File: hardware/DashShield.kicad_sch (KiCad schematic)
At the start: 60 parts, among them J1 GPIO, J2 Steering Wheel, J3 Dash LEDs, J4 CAN 0, J5 PWR, J6 CAN 1, Q1 2N7002, Q2 2N7002, Q3 2N7002, Q4 2N7002, Q5 2N7002, Q6 2N7002, U1 CAT24C256, U2 MCP2562-E-SN, U3 MCP2515-xST, U4 MCP2515-xST, U5 MCP2562-E-SN, Y1 8MHz, Y2 8MHz

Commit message: feat: finish power supply
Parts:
- added C14, C15, C16, C19: 10uF, symbol Device:C_Polarized
- added C17, C18: 100nF, symbol Device:C
- added C20: 10nF, symbol Device:C
- added D6: CRS15, Diode_SMD:D_SOD-123F, symbol Device:D
- added R18, R20, R21, R22: 10k, symbol Device:R
- added U6: ~, U3V40x:U3V40x, symbol U3V40x:U3V40F5
- R16: value 3.3Ω -> 3.3
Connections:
- net +5V: now also C15.1, C16.1, C17.1, C18.1, C19.1, C20.1, U6. (~{EN})
- net GND: now also C14.2, C15.2, C16.2, C17.2, C18.2, C19.2, C20.2, R18.1, R22.1, U6. (~{EN})
- net VS: now also C14.1, D6.1 (K), R20.2, U6. (~{EN})
- net +BATT: now reaches C12.1, D2.1 (K), D5.2 (A), R15.2, R16.1, R19.2
- net +BATT: now also D6.2 (A), R21.2
- new net VBATT Sense: R21.1, R22.2
- new net VIN Sense: R18.2, R20.1
- no-connect marks 15 -> 16
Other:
- note added: "Additional Decoupling Capacitors"
- note added: "Power Loss Detection"
- moved on the sheet: C12, C13, D1, D2, D3, D4, D5, J5, R15, R16, R17, R19

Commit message: feat: initial revision of dash PCB schematic
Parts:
- removed J4: CAN 0, symbol Connector_Generic_Shielded:Conn_01x02_Shielded
- removed J6: CAN 1, symbol Connector_Generic_Shielded:Conn_01x02_Shielded
- removed JP1: ID_WP, symbol Jumper:SolderJumper_2_Open
- added C21, C22: 10nF, Capacitor_SMD:C_0603_1608Metric, symbol Device:C
- added J4: CAN0, Connector_Molex:Molex_Micro-Fit_3.0_43650-0315_1x03_P3.00mm_Vertical, symbol Connector_Generic:Conn_01x03
- added J7: CAN1, Connector_Molex:Molex_Micro-Fit_3.0_43650-0315_1x03_P3.00mm_Vertical, symbol Connector_Generic:Conn_01x03
- added JP1: WP Enable Jumper, Connector_PinHeader_2.54mm:PinHeader_1x02_P2.54mm_Vertical, symbol Jumper:Jumper_2_Open
- added Q7, Q8, Q9: 2N7002, Package_TO_SOT_SMD:SOT-23, symbol Transistor_FET:2N7002
- added R23, R24, R25, R26, R27, R28: 270, Resistor_SMD:R_0603_1608Metric, symbol Device:R
- added R29, R30, R33: 1k, Resistor_SMD:R_0603_1608Metric, symbol Device:R
- added R31, R32, R35, R36, R37, R38, R39, R40: 10k, Resistor_SMD:R_0603_1608Metric, symbol Device:R
- C1, C10, C11, C14, C15, C16, C17, C18, C19, C2, C20, C3, C4, C5, C6, C7, C8, C9: footprint (none) -> Capacitor_SMD:C_0603_1608Metric
- C12, C13: value 10F -> 25F; footprint (none) -> Capacitor_THT:CP_Radial_D16.0mm_P7.50mm
- D1: footprint (none) -> Diode_SMD:D_SMA
- D2, D3: footprint (none) -> Package_TO_SOT_SMD:SOT-23
- D4: footprint (none) -> LED_SMD:LED_0603_1608Metric
- J2: footprint (none) -> Connector_Molex:Molex_Micro-Fit_3.0_43045-1212_2x06_P3.00mm_Vertical; symbol Connector_Generic:Conn_02x06_Counter_Clockwise -> Connector_Generic:Conn_02x06_Top_Bottom
- J3: footprint (none) -> Connector_Molex:Molex_Micro-Fit_3.0_43045-0812_2x04_P3.00mm_Vertical; symbol Connector_Generic:Conn_02x04_Counter_Clockwise -> Connector_Generic:Conn_02x04_Top_Bottom
- J5: footprint (none) -> Connector_Molex:Molex_Micro-Fit_3.0_43650-0215_1x02_P3.00mm_Vertical
- JP2, JP3, JP4, JP5: footprint (none) -> Connector_PinHeader_2.54mm:PinHeader_1x02_P2.54mm_Vertical
- R1, R10, R11, R12, R13, R14, R15, R16, R17, R19, R2, R20, R21, R3, R4, R5, R6, R7, R8, R9: footprint (none) -> Resistor_SMD:R_0603_1608Metric
- R18, R22: value 10k -> 20k; footprint (none) -> Resistor_SMD:R_0603_1608Metric
- U1: footprint (none) -> Package_SO:SOIC-8_3.9x4.9mm_P1.27mm
- Y1, Y2: footprint (none) -> Crystal:Crystal_SMD_HC49-SD
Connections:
- net GPIO12/PWM0 is gone; now on net FAST 2: J1.32 (Pin_32)
- net GPIO24 is gone; now on net CAN0 INT: J1.18 (Pin_18)
- net GPIO25 is gone; now on net CAN1 INT: J1.22 (Pin_22)
- net GPIO5 is gone; now on net FAST 0: J1.29 (Pin_29)
- net GPIO6 is gone; now on net FAST 1: J1.31 (Pin_31)
- net SLOW 0 is gone; now on net GPIO26: Q1.1 (G)
- net SLOW 1 is gone; now on net GPIO19/PCM.FS: Q2.1 (G)
- net SLOW 2 is gone; now on net GPIO13/PWM1: Q3.1 (G)
- net VBATT Sense is gone; now on net GPIO2/SDA1: R21.1, R22.2
- net VIN Sense is gone; now on net GPIO3/SCL1: R18.2, R20.1
- net +3.3V: now also J2.7 (Pin_7)
- net +3V3: now also R33.1
- net +5V: now also J3.5 (Pin_5), U6.4 (OUT); no longer J3.8 (Pin_8), U6. (~{EN})
- net +BATT: now also D2.3 (K); no longer D2.1 (K)
- net CAN0 High: now also J4.1 (Pin_1)
- net CAN0 Low: now also J4.2 (Pin_2)
- net CAN1 High: now also J7.1 (Pin_1)
- net CAN1 Low: now also J7.2 (Pin_2)
- net FAST LED 0: now also J3.6 (Pin_6); no longer J3.7 (Pin_7)
- net FAST LED 1: now also J3.7 (Pin_7); no longer J3.6 (Pin_6)
- net FAST LED 2: now also J3.8 (Pin_8); no longer J3.5 (Pin_5)
- net GND: now also D3.1 (A), U6.3 (GND), C21.2, C22.2, Q7.2 (S), Q8.2 (S), Q9.2 (S), R29.2, R30.2, R35.2, R37.2, R39.2; no longer D3.2 (A), U6. (~{EN})
- net GPIO16: now also R40.1
- net GPIO17: now also Q9.1 (G)
- net GPIO18/PCM.CLK: now also R31.1
- net GPIO20/PCM.DIN: now also R38.1
- net GPIO21/PCM.DOUT: now also R36.1
- net GPIO22: now also Q7.1 (G)
- net GPIO23: now also R32.1
- net GPIO27: now also Q8.1 (G)
- net GPIO2/SDA1: now also C22.1
- net GPIO3/SCL1: now also C21.1
- net VS: now also U6.2 (VIN); no longer U6. (~{EN})
- net at C12.2, C13.1, R15.1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: now also D2.1 (A), D3.3 (K); no longer D2.2 (A), D3.1 (K)
- net CAN0 Shield: now reaches JP3.2 (B)
- net CAN0 Shield: now also J4.3 (Pin_3)
- net at U1.7 (WP): now also JP1.1 (A)
- net TC LED 0: now reaches J2.1 (Pin_1)
- net TC LED 0: now also R23.1
- net TC Disable Button: now reaches J2.10 (Pin_10)
- net TC Disable Button: now also R39.1, R40.2
- net Radio Enable Button: now reaches J2.11 (Pin_11)
- net Radio Enable Button: now also R37.1, R38.2
- net Lap Marker Button: now reaches J2.12 (Pin_12)
- net Lap Marker Button: now also R35.1, R36.2
- net TC LED 1: now reaches J2.2 (Pin_2)
- net TC LED 1: now also R25.1
- net TC LED 2: now reaches J2.3 (Pin_3)
- net TC LED 2: now also R27.1
- net TC LED 3: now reaches J2.4 (Pin_4)
- net TC LED 3: now also R28.1
- net TC LED 4: now reaches J2.5 (Pin_5)
- net TC LED 4: now also R26.1
- net TC LED 5: now reaches J2.6 (Pin_6)
- net TC LED 5: now also R24.1
- net Wheel Slip Adjust Dial: now reaches J2.8 (Pin_8)
- net Wheel Slip Adjust Dial: now also R29.1, R31.2
- net TC Power Adjust Dial: now reaches J2.9 (Pin_9)
- net TC Power Adjust Dial: now also R30.1, R32.2
- net CAN1 Shield: now reaches JP4.2 (B)
- net CAN1 Shield: now also J7.3 (Pin_3)
- new net: Q8.3 (D), R25.2, R26.2
- new net: JP1.2 (B), R33.2
- new net: Q7.3 (D), R23.2, R24.2
- new net: Q9.3 (D), R27.2, R28.2
- no-connect marks 16 -> 19
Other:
- note added: "Steering Wheel Interface"
- moved on the sheet: C1, J1, J2, J3, Q1, Q2, Q3, Q4, Q5, Q6, R1, R2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

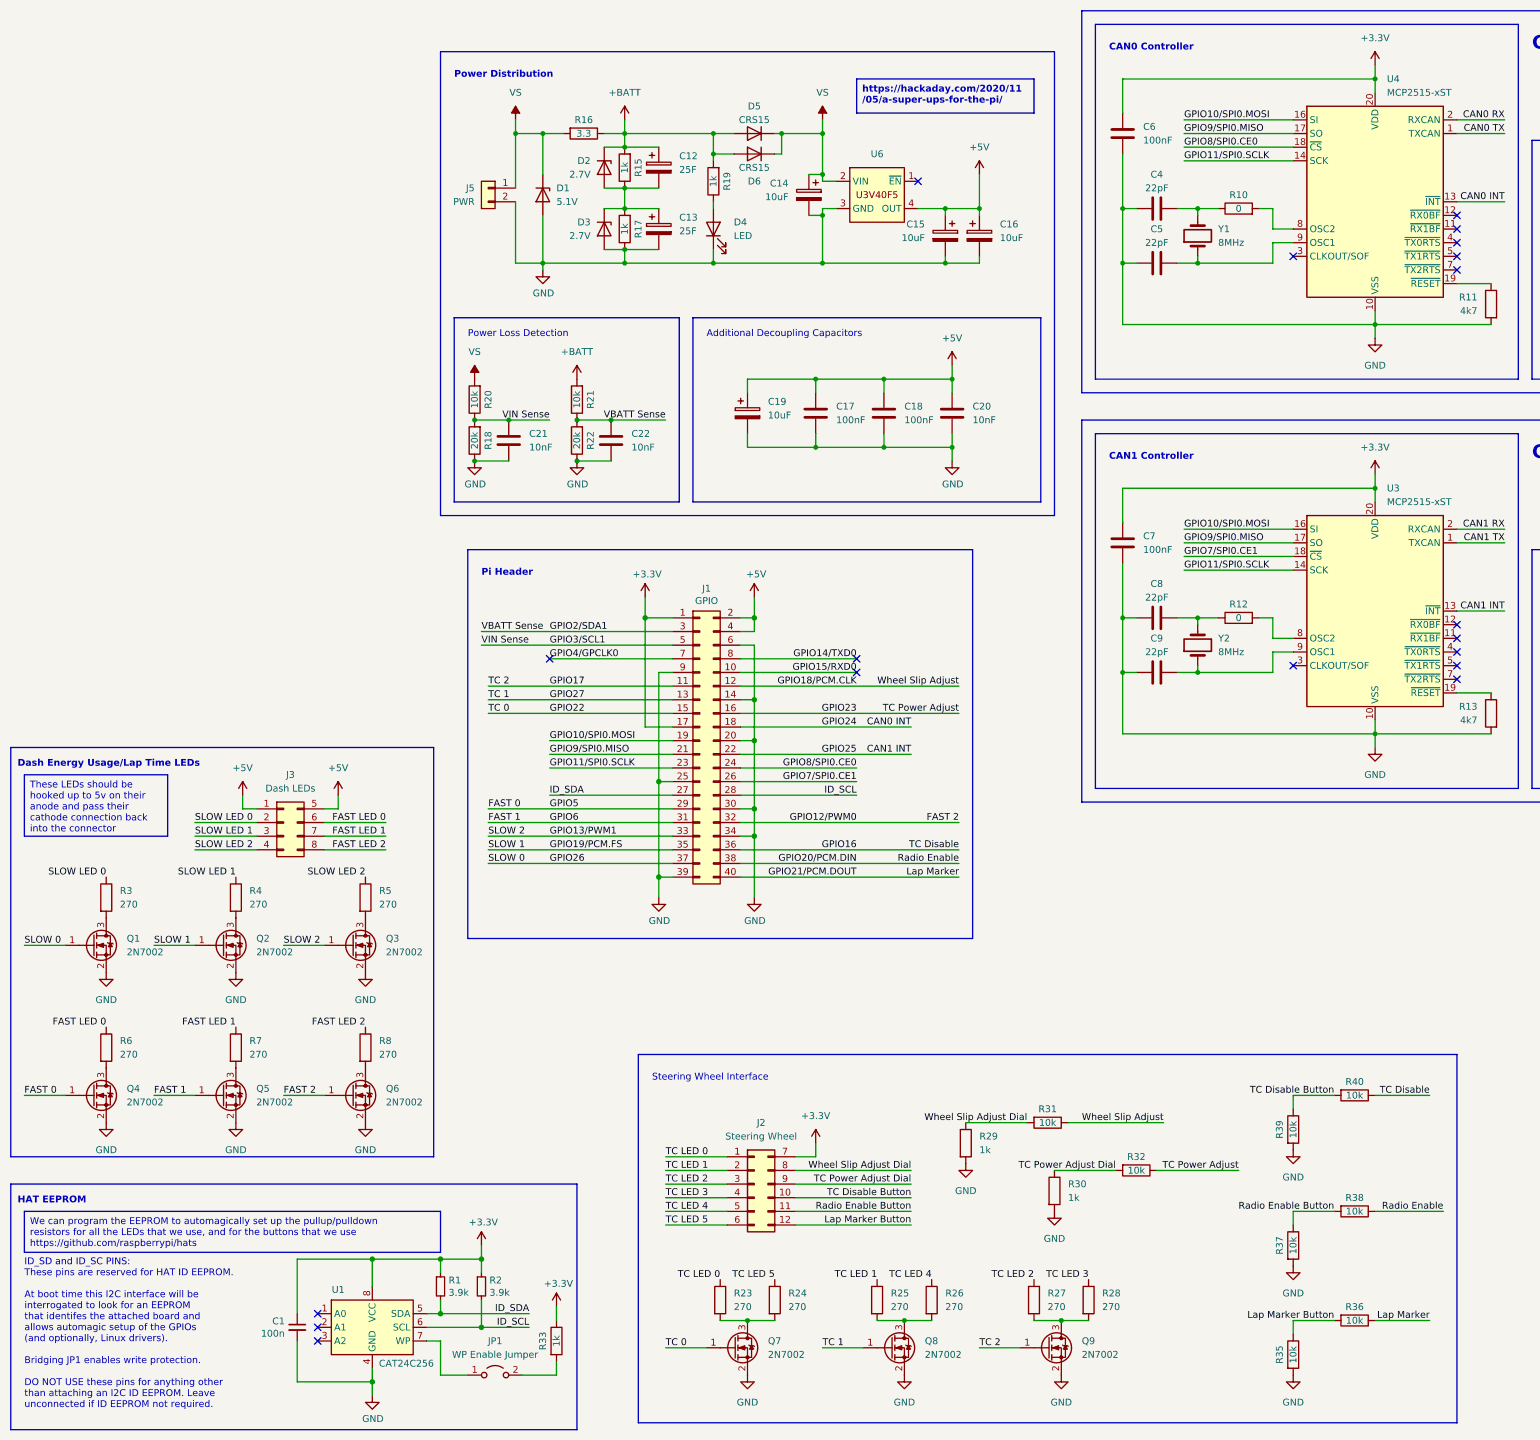
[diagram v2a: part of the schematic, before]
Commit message: feat: update steering wheel interface to 5V <-> 3.3V logic
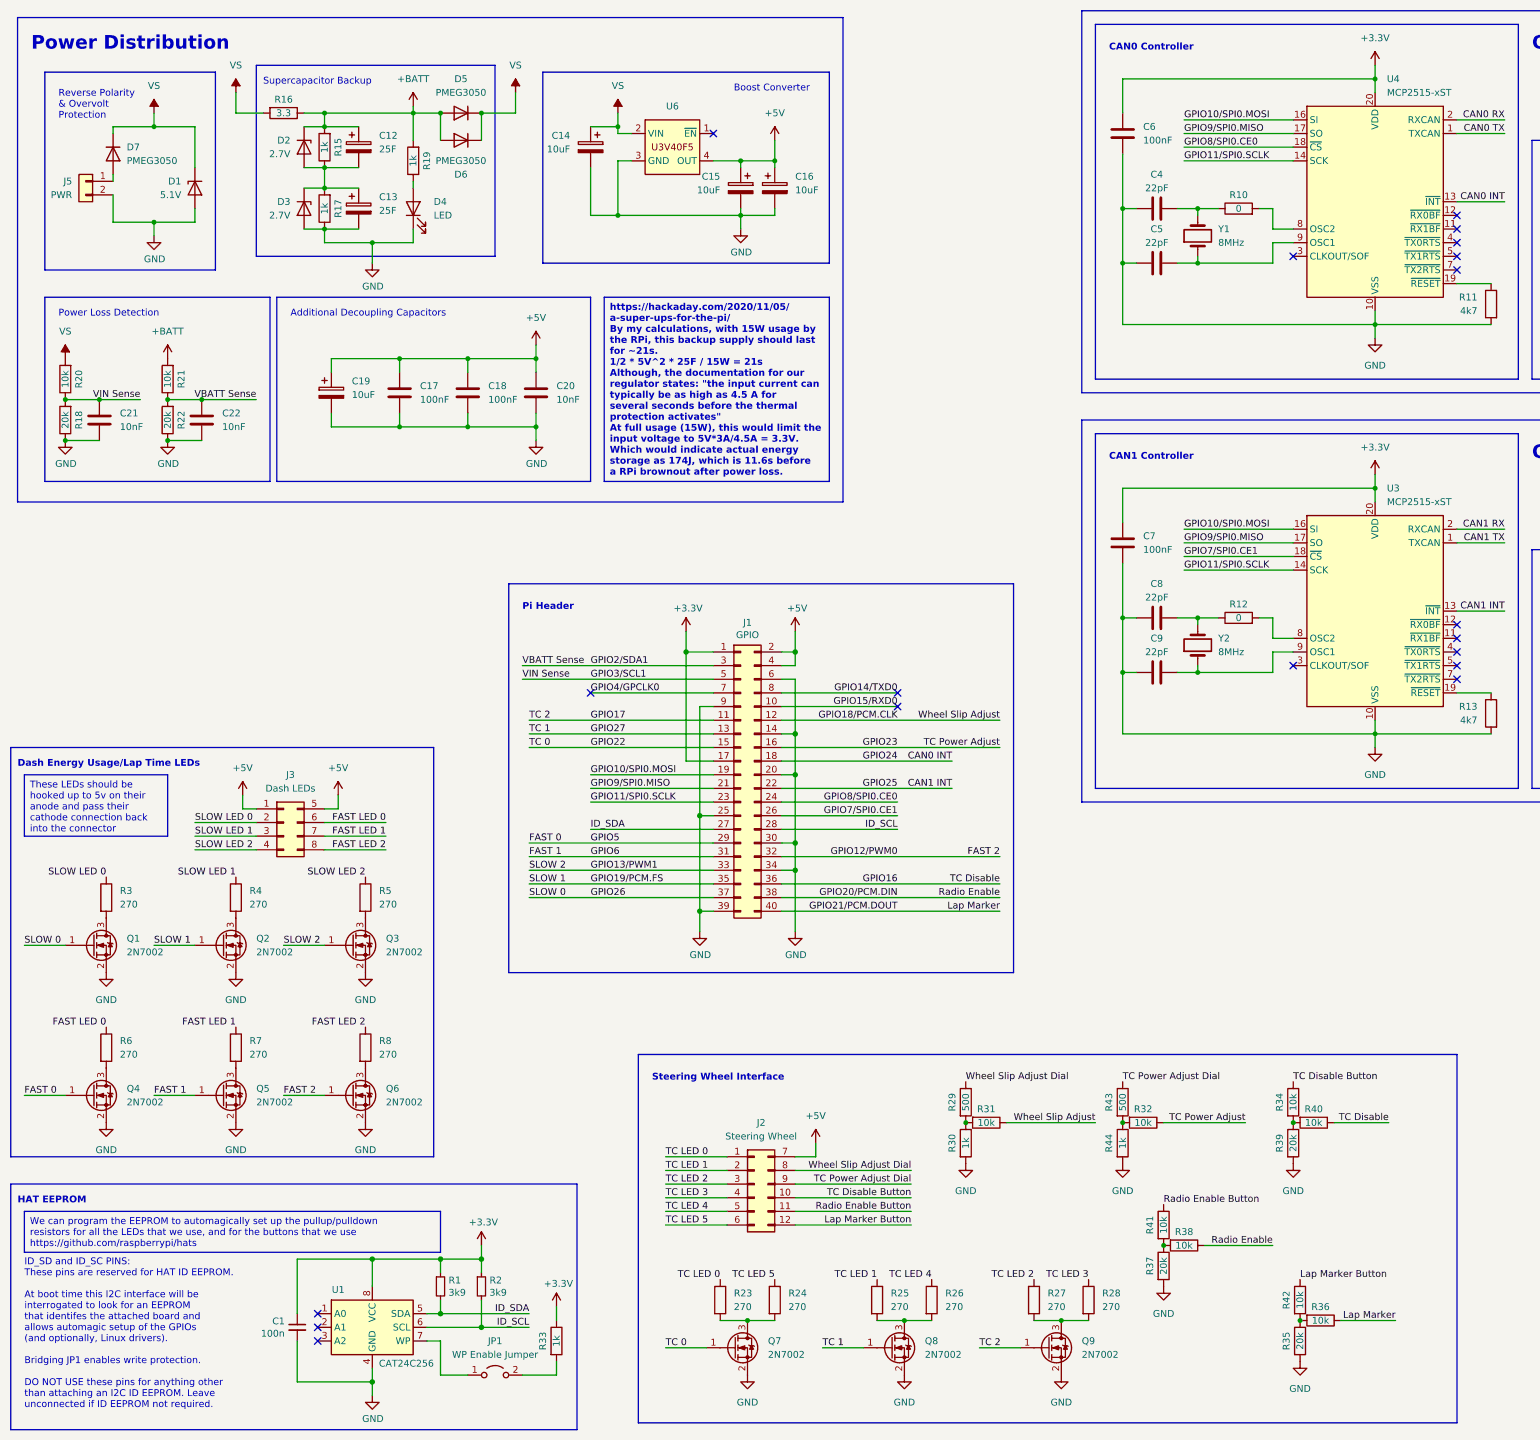
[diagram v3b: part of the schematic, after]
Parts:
- added D7: PMEG3050, Diode_SMD:D_SOD-128, symbol Device:D
- added R34, R41, R42: 10k, Resistor_SMD:R_0603_1608Metric, symbol Device:R
- added R43: 500, Resistor_SMD:R_0603_1608Metric, symbol Device:R
- added R44: 1k, Resistor_SMD:R_0603_1608Metric, symbol Device:R
- D5, D6: value CRS15 -> PMEG3050; footprint Diode_SMD:D_SOD-123F -> Diode_SMD:D_SOD-128
- R1, R2: value 3.9k -> 3k9
- R29: value 1k -> 500
- R35, R37, R39: value 10k -> 20k
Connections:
- net +3.3V: no longer J2.7 (Pin_7)
- net +5V: now also J2.7 (Pin_7)
- net GND: now also R44.2; no longer R29.2
- net Lap Marker Button: now also R42.1; no longer R35.1, R36.2
- net Radio Enable Button: now also R41.1; no longer R37.1, R38.2
- net TC Disable Button: now also R34.1; no longer R39.1, R40.2
- net TC Power Adjust Dial: now also R43.1; no longer R30.1, R32.2
- net VS: now also D7.1 (K); no longer J5.1 (Pin_1)
- net Wheel Slip Adjust Dial: no longer R31.2
- new net: R37.1, R38.2, R41.2
- new net: D7.2 (A), J5.1 (Pin_1)
- new net: R35.1, R36.2, R42.2
- new net: R34.2, R39.1, R40.2
- new net: R32.2, R43.2, R44.1
- new net: R29.2, R30.1, R31.2
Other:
- note added: "Boost Converter"
- note added: "Reverse Polarity & Overvolt Protection"
- note added: "Supercapacitor Backup"
- moved on the sheet: C12, C13, C14, C15, C16, C17, C18, C19, C20, C21, C22, D1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

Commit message: fix: apply Ayden's design review
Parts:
- removed C1: 100n, Capacitor_SMD:C_0603_1608Metric, symbol Device:C_Small
- removed J1: GPIO, Connector_PinSocket_2.54mm:PinSocket_2x20_P2.54mm_Vertical, symbol Connector_Generic:Conn_02x20_Odd_Even
- removed Q1, Q2, Q3, Q4, Q5, Q6: 2N7002, Package_TO_SOT_SMD:SOT-23, symbol Transistor_FET:2N7002
- removed R1, R2: 3k9, Resistor_SMD:R_0603_1608Metric, symbol Device:R_Small
- removed R3, R4, R5, R6, R7, R8: 270, Resistor_SMD:R_0603_1608Metric, symbol Device:R
- removed R33: 1k, Resistor_SMD:R_0603_1608Metric, symbol Device:R
- removed U1: CAT24C256, Package_SO:SOIC-8_3.9x4.9mm_P1.27mm, symbol Memory_EEPROM:CAT24C256
- added C401: 100nF, Capacitor_SMD:C_0603_1608Metric, symbol Device:C_Small
- added J601: GPIO, Connector_PinSocket_2.54mm:PinSocket_2x20_P2.54mm_Vertical, symbol Connector_Generic:Conn_02x20_Odd_Even
- added Q501, Q502, Q503, Q504, Q505, Q506: 2N7002, Package_TO_SOT_SMD:SOT-23, symbol Transistor_FET:2N7002
- added R102, R202: 0, Resistor_SMD:R_0603_1608Metric, symbol Device:R
- added R318, R321, R324, R502, R504, R506, R508, R510, R512: 10k, Resistor_SMD:R_0603_1608Metric, symbol Device:R
- added R401, R402: 3k9, Resistor_SMD:R_0603_1608Metric, symbol Device:R_Small
- added R403: 1k, Resistor_SMD:R_0603_1608Metric, symbol Device:R
- added R501, R503, R505, R507, R509, R511: 270, Resistor_SMD:R_0603_1608Metric, symbol Device:R
- added U401: CAT24C256, Package_SO:SOIC-8_3.9x4.9mm_P1.27mm, symbol Memory_EEPROM:CAT24C256
- C005: renamed from C14; footprint Capacitor_SMD:C_0603_1608Metric -> Capacitor_THT:CP_Radial_D5.0mm_P2.50mm
- C006: renamed from C15; value 10uF -> 100uF; footprint Capacitor_SMD:C_0603_1608Metric -> Capacitor_THT:CP_Radial_D5.0mm_P2.50mm
- C007: renamed from C16; footprint Capacitor_SMD:C_0603_1608Metric -> Capacitor_THT:CP_Radial_D5.0mm_P2.50mm
- C008: renamed from C19; footprint Capacitor_SMD:C_0603_1608Metric -> Capacitor_THT:CP_Radial_D5.0mm_P2.50mm
- renumbered C12 to C001, C13 to C002, C21 to C003, C22 to C004, C17 to C009, C18 to C010, C20 to C011, C6 to C101, C4 to C102, C5 to C103, C3 to C104, C2 to C105, C7 to C201, C8 to C202, C9 to C203, C10 to C204, C11 to C205, D7 to D001, D1 to D002, D2 to D003, D3 to D004, D5 to D005, D6 to D006, D4 to D007, J5 to J001, J4 to J101, J7 to J202, J2 to J301, JP2 to JP101, JP3 to JP102, JP5 to JP201, JP4 to JP202, Q7 to Q301, Q8 to Q302, Q9 to Q303, R16 to R001, R15 to R002, R17 to R003, R19 to R004, R20 to R005, R18 to R006, R21 to R007, R22 to R008, R10 to R101, R11 to R103, R9 to R104, R12 to R201, R14 to R204, R34 to R301, R39 to R302, R40 to R303, R42 to R304, R35 to R305, R36 to R306, R41 to R307, R37 to R308, R38 to R309, R29 to R310, R30 to R311, R31 to R312, R43 to R313, R44 to R314, R32 to R315, R23 to R316, R24 to R317, R25 to R319, R26 to R320, R27 to R322, R28 to R323, U6 to U001, U4 to U101, U2 to U102, U3 to U201, U5 to U202, Y1 to Y101, Y2 to Y201
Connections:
- net +3.3V: now also C401.1, J601.1 (Pin_1), J601.17 (Pin_17), R401.1, R402.1, R403.1, U401.8 (VCC)
- net +5V: now also J601.2 (Pin_2), J601.4 (Pin_4)
- net CAN0 INT: now also J601.18 (Pin_18)
- net CAN1 INT: now also J601.22 (Pin_22)
- net FAST 0: now also J601.29 (Pin_29), Q504.1 (G), R508.1
- net FAST 1: now also J601.31 (Pin_31), Q505.1 (G), R510.1
- net FAST 2: now also J601.32 (Pin_32), Q506.1 (G), R512.1
- net FAST LED 0: now also R507.1
- net FAST LED 1: now also R509.1
- net FAST LED 2: now also R511.1
- net GND: now also C401.2, J601.14 (Pin_14), J601.20 (Pin_20), J601.25 (Pin_25), J601.30 (Pin_30), J601.34 (Pin_34), J601.39 (Pin_39), J601.6 (Pin_6), J601.9 (Pin_9), Q501.2 (S), Q502.2 (S), Q503.2 (S), Q504.2 (S), Q505.2 (S), Q506.2 (S), R318.2, R321.2, R324.2, R502.2, R504.2, R506.2, R508.2, R510.2, R512.2, U401.4 (GND)
- net GPIO10/SPI0.MOSI: now also J601.19 (Pin_19)
- net GPIO11/SPI0.SCLK: now also J601.23 (Pin_23)
- net GPIO13/PWM1: now also J601.33 (Pin_33), Q503.1 (G), R506.1
- net GPIO14/TXD0: now also J601.8 (Pin_8)
- net GPIO15/RXD0: now also J601.10 (Pin_10)
- net GPIO16: now also J601.36 (Pin_36)
- net GPIO17: now also J601.11 (Pin_11), R324.1
- net GPIO18/PCM.CLK: now also J601.12 (Pin_12)
- net GPIO19/PCM.FS: now also J601.35 (Pin_35), Q502.1 (G), R504.1
- net GPIO20/PCM.DIN: now also J601.38 (Pin_38)
- net GPIO21/PCM.DOUT: now also J601.40 (Pin_40)
- net GPIO22: now also J601.15 (Pin_15), R318.1
- net GPIO23: now also J601.16 (Pin_16)
- net GPIO26: now also J601.37 (Pin_37), Q501.1 (G), R502.1
- net GPIO27: now also J601.13 (Pin_13), R321.1
- net GPIO2/SDA1: now also J601.3 (Pin_3)
- net GPIO3/SCL1: now also J601.5 (Pin_5)
- net GPIO4/GPCLK0: now also J601.7 (Pin_7)
- net GPIO7/SPI0.CE1: now also J601.26 (Pin_26)
- net GPIO8/SPI0.CE0: now also J601.24 (Pin_24)
- net GPIO9/SPI0.MISO: now also J601.21 (Pin_21)
- net ID_SCL: now also J601.28 (Pin_28), R402.2, U401.6 (SCL)
- net ID_SDA: now also J601.27 (Pin_27), R401.2, U401.5 (SDA)
- net SLOW LED 0: now also R501.1
- net SLOW LED 1: now also R503.1
- net SLOW LED 2: now also R505.1
- net at JP1.2 (B): now also R403.2
- net at JP1.1 (A): now also U401.7 (WP)
- net at C203.2, Y201.1: now also R202.2; no longer U201.9 (OSC1)
- net at C103.2, Y101.1: now also R102.2; no longer U101.9 (OSC1)
- new net: Q501.3 (D), R501.2
- new net: Q502.3 (D), R503.2
- new net: R202.1, U201.9 (OSC1)
- new net: Q504.3 (D), R507.2
- new net: Q506.3 (D), R511.2
- new net: R102.1, U101.9 (OSC1)
- new net: Q505.3 (D), R509.2
- new net: Q503.3 (D), R505.2
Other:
- note added: "Buttons"
- note added: "Dials"
- note added: "Fast Pace LEDs"
- note added: "Power Definitions"
- note added: "Slow Pace LEDs"
- note added: "TC LEDs"
- moved on the sheet: C001, C002, C003, C004, C005, C006, C007, C008, C009, C010, C011, D001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
